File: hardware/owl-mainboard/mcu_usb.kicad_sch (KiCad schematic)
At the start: 0 parts

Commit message: feat(hardware): draw the main board MCU, USB-C and button sheet
The mcu_usb sheet carries the ESP32-S3-WROOM-1-N16R8 with 22 uF + 100 nF at
its 3V3 pin, the EN network (10k, 1 uF, reset pad), the GPIO0 pull-up with
the boot pads, the 32.768 kHz crystal with 18 pF load capacitors, USB-C with
a separate 5.1k Rd per CC pin, USBLC6-2SC6, 22 ohm series resistors and the
VBUS TVS, the three buttons with 100k pull-ups and 10 nF, the J202 expansion
connector with 10k pull-ups, the UART pads, a notes box and the GPIO table.

TPS63802 PG now reaches ESP_EN through R212 (1k) on its own net TPS_PG, so
the open-drain PG output no longer discharges the 1 uF EN capacitor directly.
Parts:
- added C201: 22uF, Capacitor_SMD:C_0603_1608Metric, symbol Device:C
- added C202: 100nF, Capacitor_SMD:C_0402_1005Metric, symbol Device:C
- added C203: 1uF, Capacitor_SMD:C_0402_1005Metric, symbol Device:C
- added C204, C205: 18pF, Capacitor_SMD:C_0402_1005Metric, symbol Device:C
- added C206, C207, C208: 10nF, Capacitor_SMD:C_0402_1005Metric, symbol Device:C
- added D201: SMF5.0A, Diode_SMD:D_SOD-123F, symbol Device:D_Zener
- added J201: USB-C, Connector_USB:USB_C_Receptacle_HRO_TYPE-C-31-M-12, symbol Connector:USB_C_Receptacle_USB2.0_16P
- added J202: EXP: GND, 3V3, A, B, Connector_JST:JST_SH_SM04B-SRSS-TB_1x04-1MP_P1.00mm_Horizontal, symbol Connector_Generic_MountingPin:Conn_01x04_MountingPin
- added R201, R202: 5.1k, Resistor_SMD:R_0402_1005Metric, symbol Device:R
- added R203, R204: 22, Resistor_SMD:R_0402_1005Metric, symbol Device:R
- added R205, R206, R210, R211: 10k, Resistor_SMD:R_0402_1005Metric, symbol Device:R
- added R207, R208, R209: 100k, Resistor_SMD:R_0402_1005Metric, symbol Device:R
- added R212: 1k, Resistor_SMD:R_0402_1005Metric, symbol Device:R
- added SW201: Ear left, Button_Switch_SMD:SW_SPST_EVQP7A, symbol Switch:SW_Push
- added SW202: Ear right, Button_Switch_SMD:SW_SPST_EVQP7A, symbol Switch:SW_Push
- added SW203: Beak, Button_Switch_SMD:SW_SPST_TS-1088-xR020, symbol Switch:SW_Push
- added TP201: RESET, TestPoint:TestPoint_Pad_D1.5mm, symbol Connector:TestPoint
- added TP202: BOOT, TestPoint:TestPoint_Pad_D1.5mm, symbol Connector:TestPoint
- added TP203: GND, TestPoint:TestPoint_Pad_D1.5mm, symbol Connector:TestPoint
- added TP204: TX, TestPoint:TestPoint_Pad_D1.0mm, symbol Connector:TestPoint
- added TP205: RX, TestPoint:TestPoint_Pad_D1.0mm, symbol Connector:TestPoint
- added U201: ESP32-S3-WROOM-1-N16R8, owltunes:ESP32-S3-WROOM-1_Drill0.3, symbol RF_Module:ESP32-S3-WROOM-1
- added U202: USBLC6-2SC6, Package_TO_SOT_SMD:SOT-23-6, symbol Power_Protection:USBLC6-2SC6
- added Y201: 32.768kHz 12.5pF, Crystal:Crystal_SMD_3215-2Pin_3.2x1.5mm, symbol Device:Crystal
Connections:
- new net +3V3: C201.1, C202.1, J202.2 (Pin_2), R205.1, R206.1, R207.1, R208.1, R209.1, R210.1, R211.1, U201.2 (3V3)
- new net BOOT: R206.2, TP202.1, U201.27 (IO0)
- new net BTN_BEAK: C208.1, R209.2, SW203.1, U201.4 (IO4)
- new net BTN_EAR_L: C206.1, R207.2, SW201.1, U201.38 (IO2)
- new net BTN_EAR_R: C207.1, R208.2, SW202.1, U201.15 (IO3)
- new net CHG_PGOOD: U201.7 (IO7)
- new net CHG_STAT: U201.12 (IO8)
- new net CHG_SUSPEND: U201.26 (IO45)
- new net DISP_EN: U201.16 (IO46)
- new net DOCK_DET: U201.39 (IO1)
- new net ESP_EN: C203.1, R205.2, R212.2, TP201.1, U201.3 (EN)
- new net EXP_A: J202.3 (Pin_3), R210.2, U201.10 (IO17)
- new net EXP_B: J202.4 (Pin_4), R211.2, U201.11 (IO18)
- new net GND: C201.2, C202.2, C203.2, C204.2, C205.2, C206.2, C207.2, C208.2, D201.2 (A), J201.A1 (GND), J201.A12 (GND), J201.B1 (GND), J201.B12 (GND), J201.SH (SHIELD), J202.1 (Pin_1), J202.MP (MountPin), R201.2, R202.2, SW201.2, SW202.2, SW203.2, TP203.1, U201.1 (GND), U201.40 (GND), U201.41 (GND), U202.2 (GND)
- new net HALL_INT: U201.5 (IO5)
- new net I2C_SCL: U201.34 (IO41)
- new net I2C_SDA: U201.35 (IO42)
- new net IMU_INT1: U201.6 (IO6)
- new net LCD_CLK: U201.20 (IO12)
- new net LCD_CS: U201.18 (IO10)
- new net LCD_D0: U201.19 (IO11)
- new net LCD_D1: U201.21 (IO13)
- new net LCD_D2: U201.22 (IO14)
- new net LCD_D3: U201.17 (IO9)
- new net LCD_RST: U201.32 (IO39)
- new net LCD_TE: U201.31 (IO38)
- new net TPS_PG: R212.1
- new net TP_INT: U201.23 (IO21)
- new net TP_RST: U201.33 (IO40)
- new net TP_SCL: U201.25 (IO48)
- new net TP_SDA: U201.24 (IO47)
- new net U0RXD: TP205.1, U201.36 (RXD0)
- new net U0TXD: TP204.1, U201.37 (TXD0)
- new net USB_CC1: J201.A5 (CC1), R201.1
- new net USB_CC2: J201.B5 (CC2), R202.1
- new net USB_DM: R204.2, U201.13 (USB_D-)
- new net USB_DM_CONN: J201.A7 (D-), J201.B7 (D-), R204.1, U202.3 (I/O2), U202.4 (I/O2)
- new net USB_DP: R203.2, U201.14 (USB_D+)
- new net USB_DP_CONN: J201.A6 (D+), J201.B6 (D+), R203.1, U202.1 (I/O1), U202.6 (I/O1)
- new net VBUS_USB: D201.1 (K), J201.A4 (VBUS), J201.A9 (VBUS), J201.B4 (VBUS), J201.B9 (VBUS), U202.5 (VBUS)
- new net XTAL32_N: C205.1, U201.9 (IO16), Y201.2
- new net XTAL32_P: C204.1, U201.8 (IO15), Y201.1
- no-connect marks 0 -> 5
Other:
- note added: "32.768 kHz RTC crystal"
- note added: "Boot strap and programming pads"
- note added: "Buttons: switch to GND, 100k pull-up, 10 nF, deep-sleep wake on RTC GPIOs"
- note added: "ESP32-S3 module (U201): 3V3 decoupling, EN reset released by TPS63802 PG"
- note added: "Expansion / encoder (J202, Qwiic order)"
- note added: "GPIO map (ESP32-S3-WROOM-1-N16R8)"
- note added: "USB-C input (J201): ESD, VBUS TVS, CC pull-downs, 22 ohm series resistors"

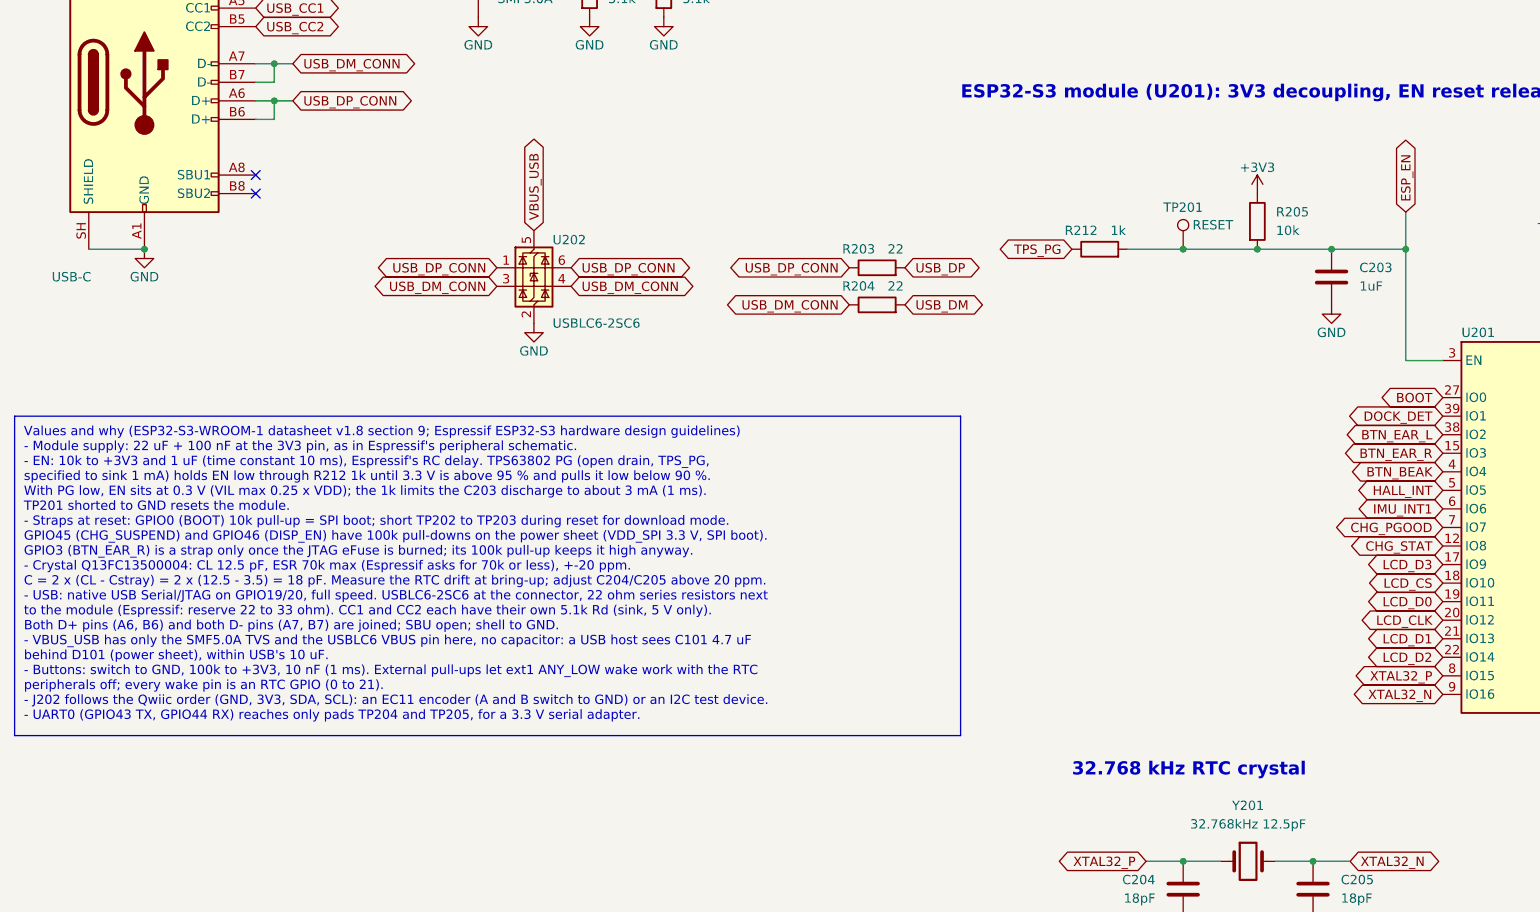
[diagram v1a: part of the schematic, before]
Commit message: fix(hardware): keep TPS63802 PG under 1 mA on the ESP32 EN network and leave the USBLC6 VBUS pin open
EN now uses R205 47k, C203 220 nF and R212 4.7k: PG sinks at most
3.3 V / 4.7k = 0.70 mA, the divider holds EN at 0.30 V or less while PG is
low, EN releases with a 10.3 ms time constant and PG glitches shorter than
about 1 ms are filtered.

U202 pin 5 is no longer tied to VBUS_USB, so the ESP32-S3's D+ pull-up
cannot back-feed the receptacle VBUS through the upper steering diode while
unplugged.

The notes boxes on both sheets state these numbers, and the mcu_usb notes
record that the U0TXD 499 ohm series resistor is inside the module.
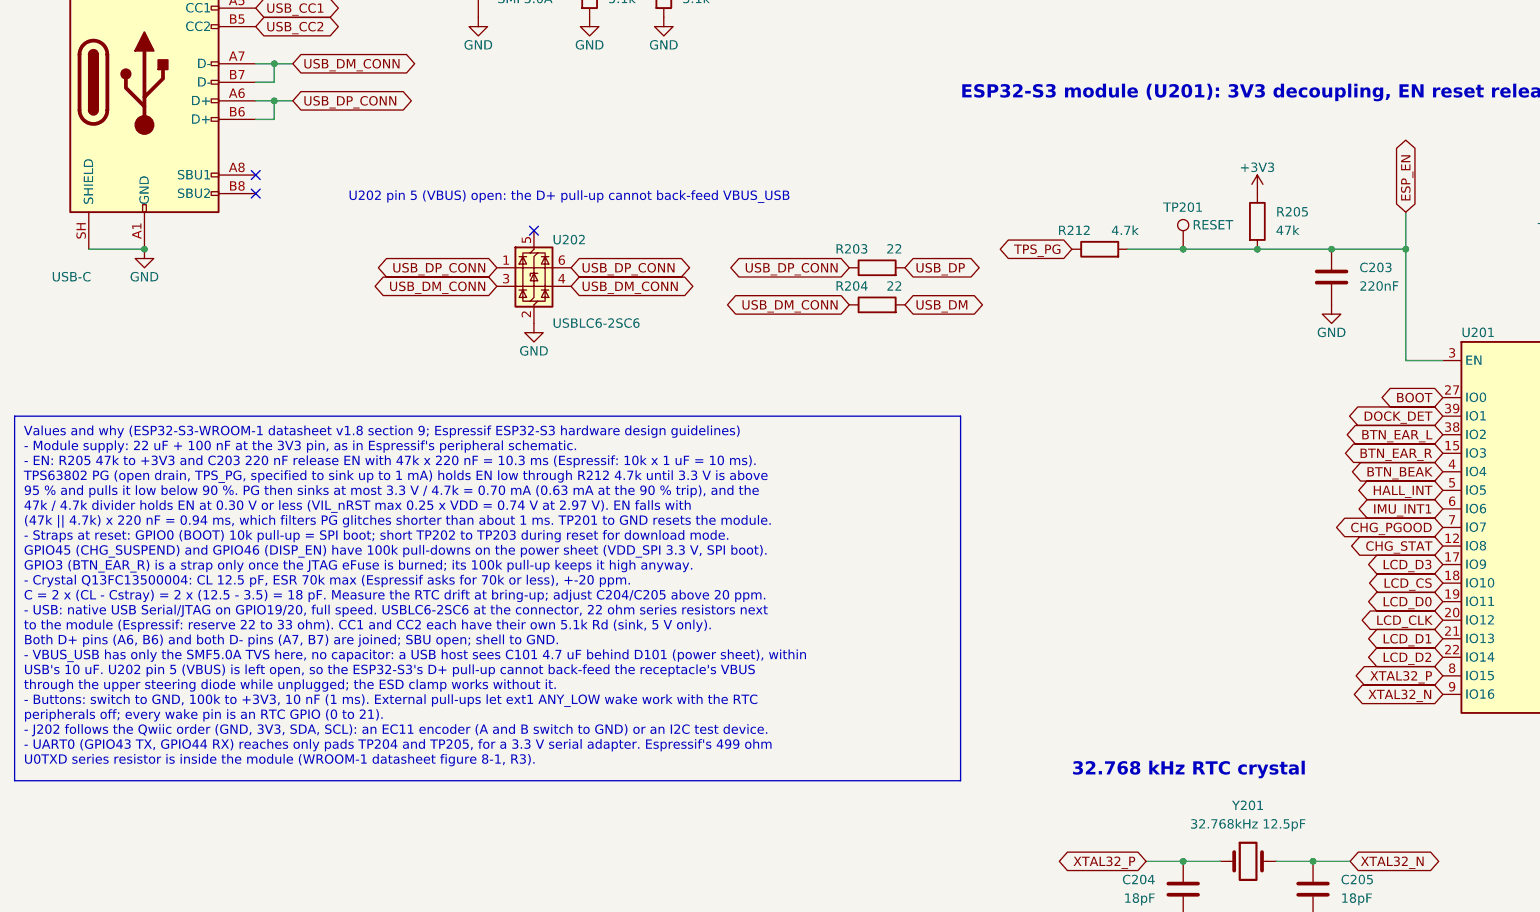
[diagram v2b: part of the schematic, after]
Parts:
- C203: value 1uF -> 220nF; LCSC Part # C52923 -> C16772; MPN CL05A105KA5NQNC -> CL05B224KO5NNNC
- R205: value 10k -> 47k; LCSC Part # C25744 -> C25792; MPN 0402WGF1002TCE -> 0402WGF4702TCE
- R212: value 1k -> 4.7k; LCSC Part # C11702 -> C25900; MPN 0402WGF1001TCE -> 0402WGF4701TCE
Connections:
- net VBUS_USB: no longer U202.5 (VBUS)
- no-connect marks 5 -> 6
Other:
- note added: "U202 pin 5 (VBUS) open: the D+ pull-up cannot back-feed VBUS_USB"
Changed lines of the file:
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@@
 		)
 	)
+	(text "U202 pin 5 (VBUS) open: the D+ pull-up cannot back-feed VBUS_USB"
+		(exclude_from_sim no)
+		(at 63.5 87.63 0)
+		(effects
+			(font
+				(size 1.27 1.27)
+			)
+			(justify left bottom)
+		)
+	)
 	(text "Expansion / encoder (J202, Qwiic order)"
 		(exclude_from_sim no)
@@
 		)
 	)
-	(text_box "Values and why (ESP32-S3-WROOM-1 datasheet v1.8 section 9; Espressif ESP32-S3 hardware design guidelines)\n- Module supply: 22 uF + 100 nF at the 3V3 pin, as in Espressif's peripheral schematic.\n- EN: 10k to +3V3 and 1 uF (time constant 10 ms), Espressif's RC delay. TPS63802 PG (open drain, TPS_PG,\n  specified to sink 1 mA) holds EN low through R212 1k until 3.3 V is above 95 % and pulls it low below 90 %.\n  With PG low, EN sits at 0.3 V (VIL max 0.25 x VDD); the 1k limits the C203 discharge to about 3 mA (1 ms).\n  TP201 shorted to GND resets the module.\n- Straps at reset: GPIO0 (BOOT) 10k pull-up = SPI boot; short TP202 to TP203 during reset for download mode.\n  GPIO45 (CHG_SUSPEND) and GPIO46 (DISP_EN) have 100k pull-downs on the power sheet (VDD_SPI 3.3 V, SPI boot).\n  GPIO3 (BTN_EAR_R) is a strap only once the JTAG eFuse is burned; its 100k pull-up keeps it high anyway.\n- Crystal Q13FC13500004: CL 12.5 pF, ESR 70k max (Espressif asks for 70k or less), +-20 ppm.\n  C = 2 x (CL - Cstray) = 2 x (12.5 - 3.5) = 18 pF. Measure the RTC drift at bring-up; adjust C204/C205 above 20 ppm.\n- USB: native USB Serial/JTAG on GPIO19/20, full speed. USBLC6-2SC6 at the connector, 22 ohm series resistors next\n  to the module (Espressif: reserve 22 to 33 ohm). CC1 and CC2 each have their own 5.1k Rd (sink, 5 V only).\n  Both D+ pins (A6, B6) and both D- pins (A7, B7) are joined; SBU open; shell to GND.\n- VBUS_USB has only the SMF5.0A TVS and the USBLC6 VBUS pin here, no capacitor: a USB host sees C101 4.7 uF\n  behind D101 (power sheet), within USB's 10 uF.\n- Buttons: switch to GND, 100k to +3V3, 10 nF (1 ms). External pull-ups let ext1 ANY_LOW wake work with the RTC\n  peripherals off; every wake pin is an RTC GPIO (0 to 21).\n- J202 follows the Qwiic order (GND, 3V3, SDA, SCL): an EC11 encoder (A and B switch to GND) or an I2C test device.\n- UART0 (GPIO43 TX, GPIO44 RX) reaches only pads TP204 and TP205, for a 3.3 V serial adapter."
+	(text_box "Values and why (ESP32-S3-WROOM-1 datasheet v1.8 section 9; Espressif ESP32-S3 hardware design guidelines)\n- Module supply: 22 uF + 100 nF at the 3V3 pin, as in Espressif's peripheral schematic.\n- EN: R205 47k to +3V3 and C203 220 nF release EN with 47k x 220 nF = 10.3 ms (Espressif: 10k x 1 uF = 10 ms).\n  TPS63802 PG (open drain, TPS_PG, specified to sink up to 1 mA) holds EN low through R212 4.7k until 3.3 V is above\n  95 % and pulls it low below 90 %. PG then sinks at most 3.3 V / 4.7k = 0.70 mA (0.63 mA at the 90 % trip), and the\n  47k / 4.7k divider holds EN at 0.30 V or less (VIL_nRST max 0.25 x VDD = 0.74 V at 2.97 V). EN falls with\n  (47k || 4.7k) x 220 nF = 0.94 ms, which filters PG glitches shorter than about 1 ms. TP201 to GND resets the module.\n- Straps at reset: GPIO0 (BOOT) 10k pull-up = SPI boot; short TP202 to TP203 during reset for download mode.\n  GPIO45 (CHG_SUSPEND) and GPIO46 (DISP_EN) have 100k pull-downs on the power sheet (VDD_SPI 3.3 V, SPI boot).\n  GPIO3 (BTN_EAR_R) is a strap only once the JTAG eFuse is burned; its 100k pull-up keeps it high anyway.\n- Crystal Q13FC13500004: CL 12.5 pF, ESR 70k max (Espressif asks for 70k or less), +-20 ppm.\n  C = 2 x (CL - Cstray) = 2 x (12.5 - 3.5) = 18 pF. Measure the RTC drift at bring-up; adjust C204/C205 above 20 ppm.\n- USB: native USB Serial/JTAG on GPIO19/20, full speed. USBLC6-2SC6 at the connector, 22 ohm series resistors next\n  to the module (Espressif: reserve 22 to 33 ohm). CC1 and CC2 each have their own 5.1k Rd (sink, 5 V only).\n  Both D+ pins (A6, B6) and both D- pins (A7, B7) are joined; SBU open; shell to GND.\n- VBUS_USB has only the SMF5.0A TVS here, no capacitor: a USB host sees C101 4.7 uF behind D101 (power sheet), within\n  USB's 10 uF. U202 pin 5 (VBUS) is left open, so the ESP32-S3's D+ pull-up cannot back-feed the receptacle's VBUS\n  through the upper steering diode while unplugged; the ESD clamp works without it.\n- Buttons: switch to GND, 100k to +3V3, 10 nF (1 ms). External pull-ups let ext1 ANY_LOW wake work with the RTC\n  peripherals off; every wake pin is an RTC GPIO (0 to 21).\n- J202 follows the Qwiic order (GND, 3V3, SDA, SCL): an EC11 encoder (A and B switch to GND) or an I2C test device.\n- UART0 (GPIO43 TX, GPIO44 RX) reaches only pads TP204 and TP205, for a 3.3 V serial adapter. Espressif's 499 ohm\n  U0TXD series resistor is inside the module (WROOM-1 datasheet figure 8-1, R3)."
 		(exclude_from_sim no)
 		(at 17.78 116.84 0)
-		(size 129.54 43.74)
+		(size 129.54 49.92)
 		(margins 1.27 1.27 1.27 1.27)
 		(stroke
@@
 	)
 	(no_connect
+		(at 88.9 91.44)
+	)
+	(no_connect
 		(at 50.8 86.36)
 	)
@@
 		)
 	)
-	(global_label "VBUS_USB"
-		(shape bidirectional)
-		(at 88.9 91.44 90)
-		(effects
-			(font
-				(size 1.27 1.27)
-			)
-			(justify left)
-		)
-		(property "Intersheetrefs" "${INTERSHEET_REFS}"
-			(at 88.9 91.44 0)
-			(hide yes)
-			(show_name no)
-			(do_not_autoplace no)
-			(effects
-				(font
-					(size 1.27 1.27)
-				)
-			)
-		)
-	)
 	(global_label "CHG_STAT"
 		(shape bidirectional)
@@
 			)
 		)
-		(property "Value" "10k"
+		(property "Value" "47k"
 			(at 190.5 91.44 0)
 			(show_name no)
@@
 			)
 		)
-		(property "LCSC Part #" "C25744"
+		(property "LCSC Part #" "C25792"
 			(at 187.96 90.17 0)
 			(hide yes)
@@
 			)
 		)
-		(property "MPN" "0402WGF1002TCE"
+		(property "MPN" "0402WGF4702TCE"
 			(at 187.96 90.17 0)
 			(hide yes)
@@
 		(dnp no)
 		(property "Reference" "R212"
-			(at 163.83 91.44 90)
+			(at 162.9 91.44 90)
 			(show_name no)
 			(do_not_autoplace no)
@@
 			)
 		)
-		(property "Value" "1k"
-			(at 168.91 91.44 90)
+		(property "Value" "4.7k"
+			(at 169.84 91.44 90)
 			(show_name no)
 			(do_not_autoplace no)
@@
 			)
 		)
-		(property "LCSC Part #" "C11702"
+		(property "LCSC Part #" "C25900"
 			(at 166.37 93.98 0)
 			(hide yes)
@@
 			)
 		)
-		(property "MPN" "0402WGF1001TCE"
+		(property "MPN" "0402WGF4701TCE"
 			(at 166.37 93.98 0)
 			(hide yes)
@@
 		(dnp no)
 		(property "Reference" "R204"
-			(at 133.35 99.06 90)
+			(at 132.42 99.06 90)
 			(show_name no)
 			(do_not_autoplace no)
@@
 		)
 		(property "Value" "22"
-			(at 138.43 99.06 90)
+			(at 138.26 99.06 90)
 			(show_name no)
 			(do_not_autoplace no)
@@
 		(dnp no)
 		(property "Reference" "R203"
-			(at 133.35 93.98 90)
+			(at 132.42 93.98 90)
 			(show_name no)
 			(do_not_autoplace no)
@@
 		)
 		(property "Value" "22"
-			(at 138.43 93.98 90)
+			(at 138.26 93.98 90)
 			(show_name no)
 			(do_not_autoplace no)
@@
 			)
 		)
-		(property "Value" "1uF"
+		(property "Value" "220nF"
 			(at 201.93 99.06 0)
 			(show_name no)
@@
 			)
 		)
-		(property "LCSC Part #" "C52923"
+		(property "LCSC Part #" "C16772"
 			(at 198.12 97.79 0)
 			(hide yes)
@@
 			)
 		)
-		(property "MPN" "CL05A105KA5NQNC"
+		(property "MPN" "CL05B224KO5NNNC"
 			(at 198.12 97.79 0)
 			(hide yes)

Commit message: fix(hardware): set the JLC rotation offsets the EasyEDA footprints call for
Each assembled part's EasyEDA footprint (JLC's placement zero) was matched pad by pad with
the KiCad footprint on the board. The Fabrication Toolkit writes a bottom rotation as 180
minus the KiCad rotation (the rotation seen from below, board turned over left to right,
true for all 81 bottom parts) plus its own table rotation, so a part needs the
EasyEDA-to-KiCad angle less the table's angle. Five parts get an FT Rotation Offset:

- D101, D102 (PMEG2020EH, C456104): 180. EasyEDA's footprint has pad 1, the cathode, on
  the right at zero; KiCad's D_SOD-123F has it on the left. No toolkit rule. CPL 180 -> 0.
- J101 (S2B-PH-SM4-TB, C295747): 180. EasyEDA's footprint matches KiCad's at zero; the
  toolkit's ^JST_PH_S rule adds 180, which this cancels. CPL 270 -> 90.
- U202 (USBLC6-2SC6, C7519): 90. EasyEDA's SOT-23-6 BL footprint (pin 1 bottom left, rows
  horizontal) is 270 from KiCad's; the toolkit's ^SOT-23 rule gives 180. CPL 180 -> 270.
- U303 (LIS2DW12TR, C189624): 270. EasyEDA's LGA-12 BL footprint runs pins 1 to 4 along
  the bottom, KiCad's down the left (ruling R30); no toolkit rule. CPL 180 -> 90.

The offsets live in design.toml (rotation_offset) and on the symbols; hw_sync.py now copies
the field to the footprint, where the toolkit reads it, hw_bom.py checks symbol against
design.toml and a test checks footprint against design.toml. JLC's placement preview
confirms them at order time. ordering.md and the review record the offsets and the method.

ERC 0, DRC 0/0/0 with parity, hw_fab 0 errors (top 6, bottom 81), Gerbers unchanged.
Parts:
- U202: FT Rotation Offset (none) -> 90
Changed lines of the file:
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@@
+			)
+		)
+		(property "FT Rotation Offset" "90"
+			(at 88.9 96.52 0)
+			(hide yes)
+			(show_name no)
+			(do_not_autoplace no)
+			(effects
+				(font
+					(size 1.27 1.27)
+				)
 			)
 		)
